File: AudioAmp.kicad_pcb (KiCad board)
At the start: 2 copper layers, 134 x 38 mm, 56 parts, among them J1 ACJS-MHOM, J2 ACJS-MHOM, Q1 MJE182G, Q12 MMBT5401, Q13 MMBT5401, Q2 MJE172G, Q3 MMBT5551(RANGE:200-300), Q9 MMBT5551(RANGE:200-300)

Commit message: PCB fertig gemacht.
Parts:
- removed H6: VCC _GND, MountingHole:MountingHole_2.5mm_Pad
- moved TP8 130.4 mm to (195.0, 92.8)
- moved TP10 101.7 mm to (151.4, 123.2)
- moved H3 97.3 mm to (175.2, 92.5)
- moved H4 93.5 mm to (166.0, 123.0)
- moved D10 83.8 mm to (170.3, 110.9), turned to 180 degrees
- moved C9 80.7 mm to (162.3, 91.0), turned to 180 degrees
- moved R12 78.5 mm to (176.5, 119.5)
- moved C2 75.6 mm to (171.7, 117.6), turned to -90 degrees
- moved TP5 70.5 mm to (156.8, 91.0)
- moved R10 70.3 mm to (119.0, 115.0)
- moved C4 69.1 mm to (151.4, 119.2), turned to 90 degrees
- moved J2 67.7 mm to (182.3, 101.1)
- moved R15 66.4 mm to (113.5, 122.5)
- moved C7 65.6 mm to (112.0, 113.0)
- moved R9 64.7 mm to (113.5, 117.0)
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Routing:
- net Net-(C1-Pad2): track 115.0 -> 28.7 mm
- net Net-(D10-A): track 12.4 -> 90.3 mm, vias 0 -> 4
- net Net-(D1-A): track 68.2 -> 128.5 mm, vias 0 -> 2
- net Net-(D9-K): track 19.2 -> 64.2 mm
- net Net-(Q13-C): track 19.7 -> 64.0 mm
- net Net-(D1-K): track 4.68 -> 43.8 mm
- net Net-(D4-A): track 0.00 -> 37.4 mm
- net Net-(Q12-E): track 14.3 -> 35.5 mm, vias 0 -> 2
- net Net-(H1-Pad1): track 28.5 -> 8.61 mm
- net Net-(D2-K): track 9.26 -> 21.0 mm
- net Net-(Q3-B): track 0.00 -> 10.2 mm
- net Net-(D2-A): track 35.3 -> 25.3 mm
- net Net-(Q9-E): track 0.00 -> 8.83 mm
- net Net-(Q1-E): track 4.50 -> 13.2 mm
- net Net-(C6-Pad1): track 13.2 -> 6.86 mm
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- added copper zone on B.Cu, net Net-(C1-Pad2)
- added copper zone on F.Cu, net Net-(C1-Pad2)
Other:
- board size 134 x 38 mm -> 145 x 40 mm

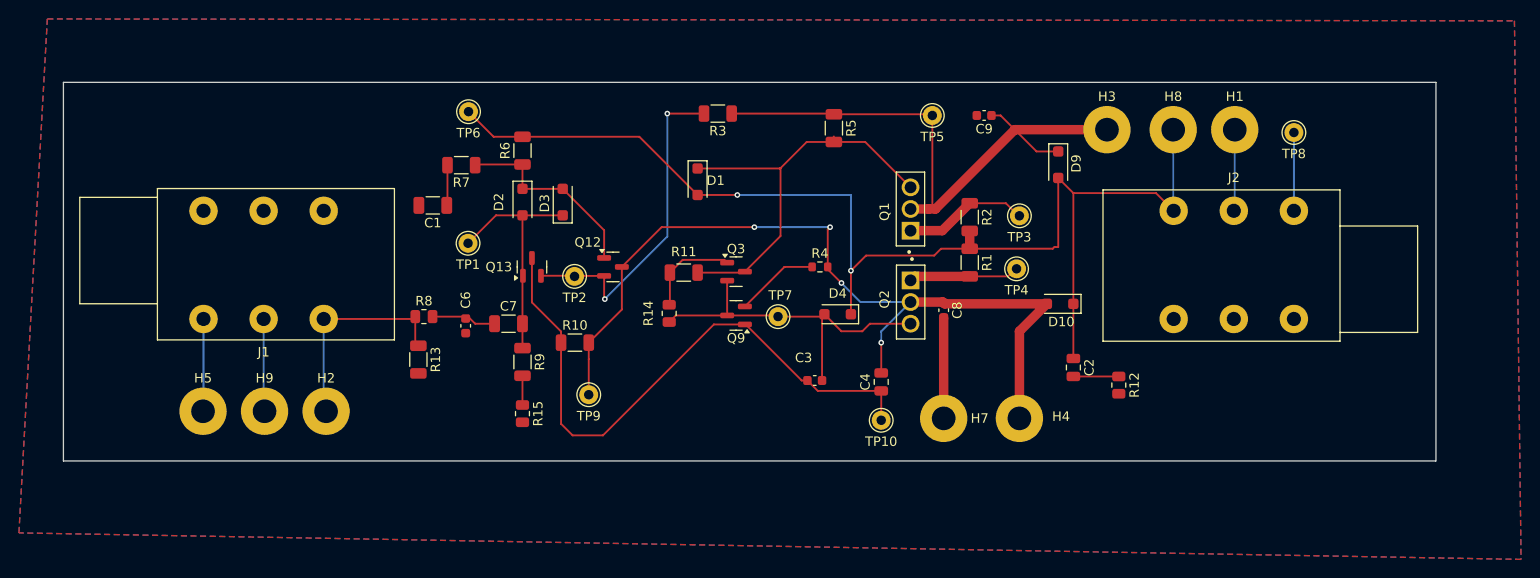
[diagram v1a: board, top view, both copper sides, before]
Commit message: CHA: Leitung zu Hochstrom erhöht
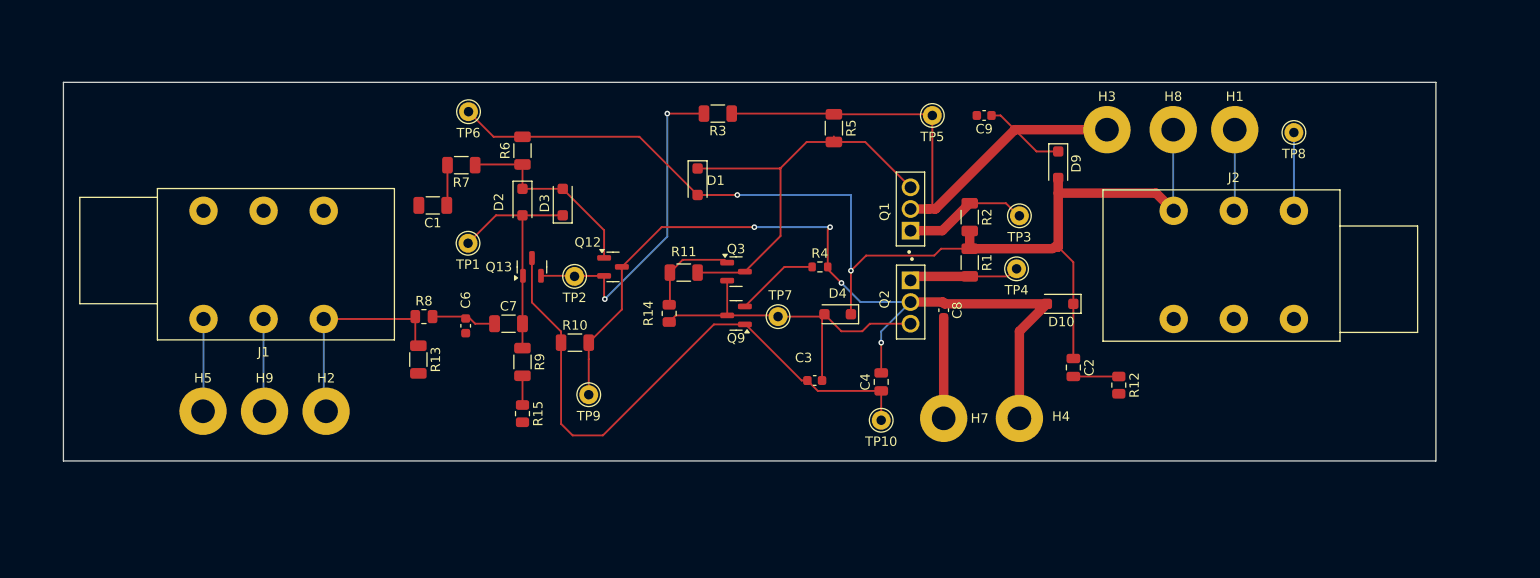
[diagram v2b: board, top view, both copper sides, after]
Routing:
- net Net-(D1-A): track 128.5 -> 122.8 mm
- removed copper zone on B.Cu, net Net-(C1-Pad2)
- removed copper zone on F.Cu, net Net-(C1-Pad2)
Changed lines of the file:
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@@
 		(start 169.525 105.075)
 		(end 160.75 105.075)
-		(width 0.2)
+		(width 1)
 		(layer "F.Cu")
 		(net 4)
@@
 	)
 	(segment
+		(start 171.7 106.5)
+		(end 170.1 104.9)
+		(width 0.2)
+		(layer "F.Cu")
+		(net 4)
+	)
+	(segment
 		(start 170.1 97.6)
 		(end 170.1 104.9)
-		(width 0.2)
+		(width 1)
 		(layer "F.Cu")
 		(net 4)
@@
 		(start 182.3 101.07)
 		(end 180.43 99.2)
-		(width 0.2)
+		(width 1)
 		(layer "F.Cu")
 		(net 4)
@@
 	)
 	(segment
-		(start 180.43 99.2)
-		(end 171.7 99.2)
-		(width 0.2)
-		(layer "F.Cu")
-		(net 4)
-	)
-	(segment
 		(start 113.5 93.25)
 		(end 110.45 93.25)
@@
 	)
 	(segment
-		(start 171.7 99.2)
-		(end 170.1 97.6)
-		(width 0.2)
-		(layer "F.Cu")
-		(net 4)
-	)
-	(segment
 		(start 132 99.4)
 		(end 136.2 99.4)
@@
 	)
 	(segment
+		(start 180.43 99.2)
+		(end 170.1 99.2)
+		(width 1)
+		(layer "F.Cu")
+		(net 4)
+	)
+	(segment
 		(start 157.725 105.075)
 		(end 160.75 105.075)
@@
 	)
 	(segment
-		(start 171.7 110.9)
-		(end 171.7 99.2)
-		(width 0.2)
-		(layer "F.Cu")
-		(net 4)
-	)
-	(segment
 		(start 160.75 103.2)
 		(end 160.75 105.075)
@@
 	)
 	(segment
+		(start 171.7 110.9)
+		(end 171.7 106.5)
+		(width 0.2)
+		(layer "F.Cu")
+		(net 4)
+	)
+	(segment
 		(start 170.1 104.9)
 		(end 169.7 104.9)
-		(width 0.2)
+		(width 1)
 		(layer "F.Cu")
 		(net 4)
@@
 		(net 27)
 	)
-	(zone
-		(net 2)
-		(net_name "Net-(C1-Pad2)")
-		(layers "F.Cu" "B.Cu")
-		(hatch edge 0.5)
-		(connect_pads
-			(clearance 0.5)
-		)
-		(min_thickness 0.25)
-		(filled_areas_thickness no)
-		(fill yes
-			(thermal_gap 0.5)
-			(thermal_bridge_width 0.5)
-		)
-		(polygon
-			(pts
-				(xy 63.3 80.8) (xy 218.3 81) (xy 219 137.9) (xy 60.3 135.1)
-			)
-		)
-	)
 	(embedded_fonts no)

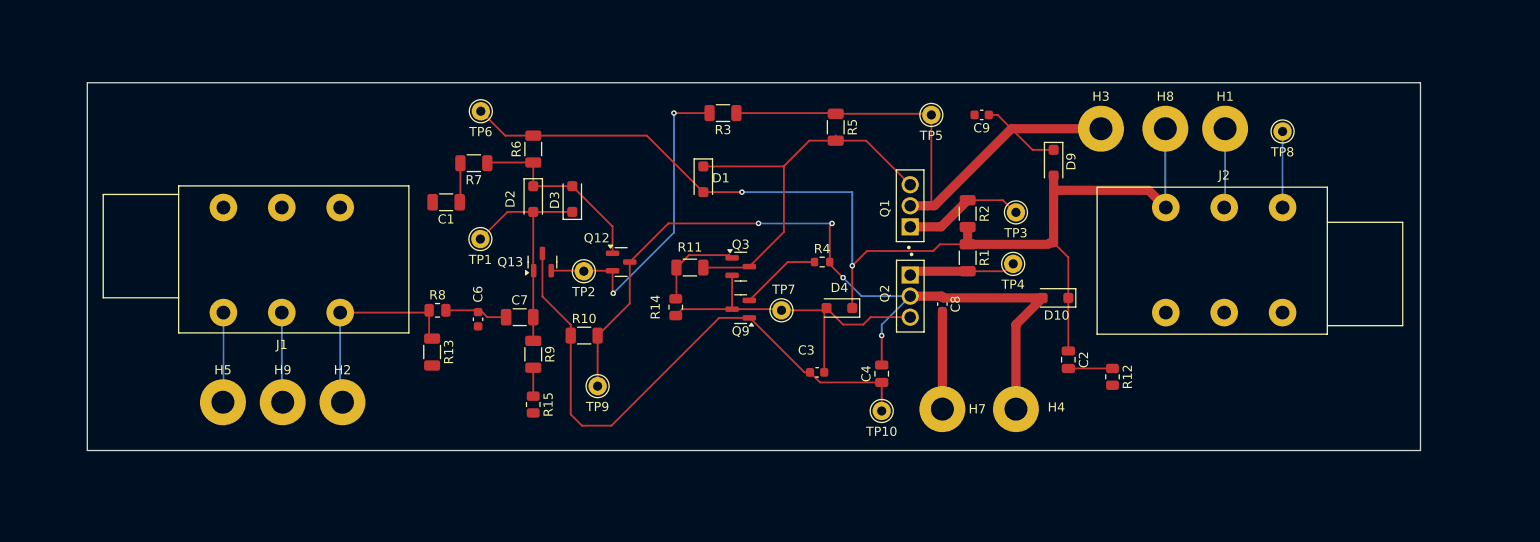
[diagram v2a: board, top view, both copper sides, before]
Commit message: Neues GND Netz gesetz und angeschlossen, Planinen rev hinzugefügt
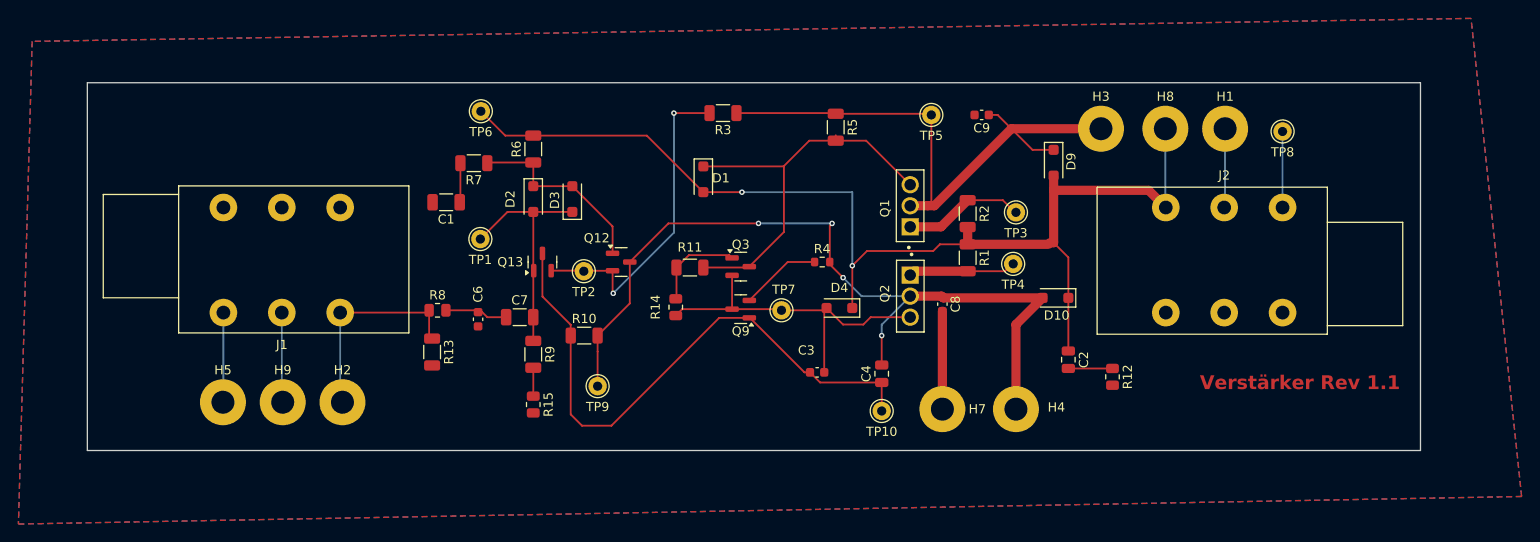
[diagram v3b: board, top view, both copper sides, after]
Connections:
- net Net-(C1-Pad2) renamed /GND
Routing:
- added copper zone on B.Cu, net /GND
- added copper zone on F.Cu, net /GND
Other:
- board text added: "Verstärker Rev 1.1"
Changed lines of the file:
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@@
 	(net 0 "")
 	(net 1 "Net-(C1-Pad1)")
-	(net 2 "Net-(C1-Pad2)")
+	(net 2 "/GND")
 	(net 3 "Net-(C2-Pad2)")
 	(net 4 "Net-(D1-A)")
@@
 			(layers "*.Cu" "*.Mask")
 			(remove_unused_layers no)
-			(net 2 "Net-(C1-Pad2)")
+			(net 2 "/GND")
 			(pinfunction "1")
 			(pintype "passive")
@@
 			(layers "F.Cu" "F.Mask" "F.Paste")
 			(roundrect_rratio 0.222222)
-			(net 2 "Net-(C1-Pad2)")
+			(net 2 "/GND")
 			(pintype "passive")
 		)
@@
 			(layers "F.Cu" "F.Mask" "F.Paste")
 			(roundrect_rratio 0.243902)
-			(net 2 "Net-(C1-Pad2)")
+			(net 2 "/GND")
 			(pintype "passive")
 		)
@@
 			(layers "*.Cu" "*.Mask")
 			(remove_unused_layers no)
-			(net 2 "Net-(C1-Pad2)")
+			(net 2 "/GND")
 			(pinfunction "1")
 			(pintype "input")
@@
 			(layers "F.Cu" "F.Mask" "F.Paste")
 			(roundrect_rratio 0.25)
-			(net 2 "Net-(C1-Pad2)")
+			(net 2 "/GND")
 			(pintype "passive")
 		)
@@
 			(layers "*.Cu" "*.Mask")
 			(remove_unused_layers no)
-			(net 2 "Net-(C1-Pad2)")
+			(net 2 "/GND")
 			(pinfunction "1")
 			(pintype "input")
@@
 			(layers "F.Cu" "F.Mask" "F.Paste")
 			(roundrect_rratio 0.25)
-			(net 2 "Net-(C1-Pad2)")
+			(net 2 "/GND")
 			(pintype "passive")
 		)
@@
 			(layers "F.Cu" "F.Mask" "F.Paste")
 			(roundrect_rratio 0.217391)
-			(net 2 "Net-(C1-Pad2)")
+			(net 2 "/GND")
 			(pintype "passive")
 		)
@@
 			(layers "F.Cu" "F.Mask" "F.Paste")
 			(roundrect_rratio 0.243902)
-			(net 2 "Net-(C1-Pad2)")
+			(net 2 "/GND")
 			(pintype "passive")
 		)
@@
 			(layers "*.Cu" "*.Mask")
 			(remove_unused_layers no)
-			(net 2 "Net-(C1-Pad2)")
+			(net 2 "/GND")
 			(pintype "passive")
 		)
@@
 			(layers "F.Cu" "F.Mask" "F.Paste")
 			(roundrect_rratio 0.25)
-			(net 2 "Net-(C1-Pad2)")
+			(net 2 "/GND")
 			(pintype "passive")
 		)
@@
 			(layers "*.Cu" "*.Mask")
 			(remove_unused_layers no)
-			(net 2 "Net-(C1-Pad2)")
+			(net 2 "/GND")
 			(pintype "passive")
 		)
@@
 		(layer "Edge.Cuts")
 	)
+	(gr_text "Verstärker Rev 1.1"
+		(at 186 121 0)
+		(layer "F.Cu")
+		(effects
+			(font
+				(size 1.5 1.5)
+				(thickness 0.3)
+				(bold yes)
+			)
+			(justify left bottom)
+		)
+	)
 	(gr_text "In"
 		(at 82.7125 108.0375 90)
@@
 		(net 27)
 	)
+	(zone
+		(net 2)
+		(net_name "/GND")
+		(layers "F.Cu" "B.Cu")
+		(hatch full 0.5)
+		(connect_pads
+			(clearance 0.5)
+		)
+		(min_thickness 0.25)
+		(filled_areas_thickness no)
+		(fill yes
+			(thermal_gap 0.5)
+			(thermal_bridge_width 0.5)
+		)
+		(polygon
+			(pts
+				(xy 59 83) (xy 57.5 135.5) (xy 221 132.5) (xy 215.5 80.5)
+			)
+		)
+	)
 	(embedded_fonts no)

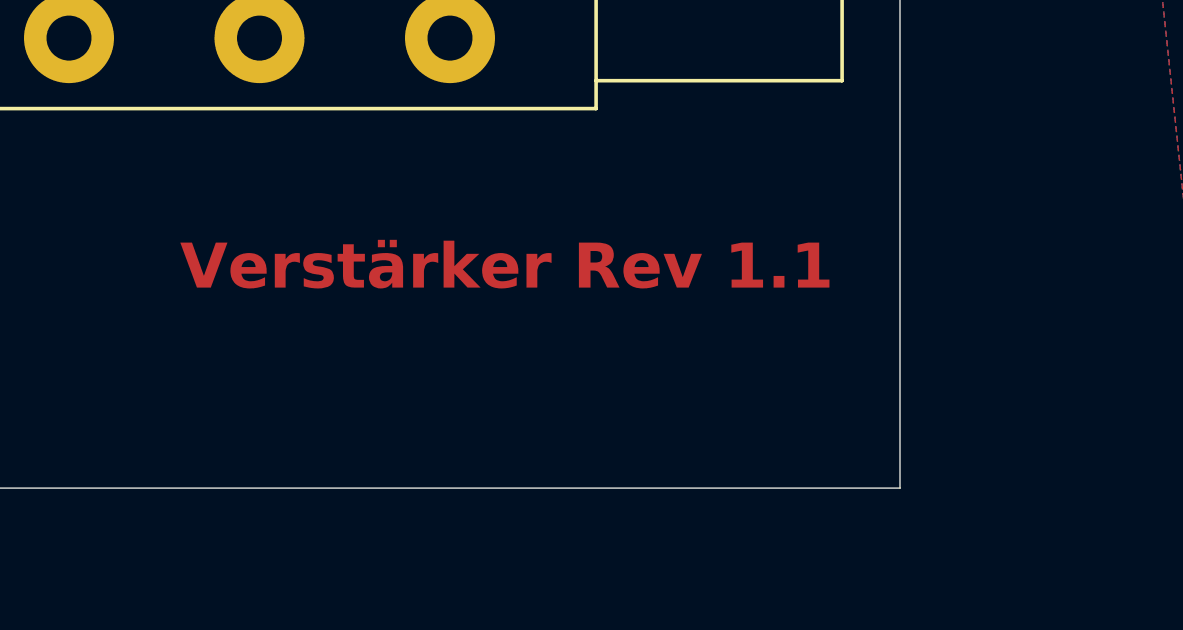
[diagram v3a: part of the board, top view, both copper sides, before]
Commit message: CHA: Projektdaten ergänzt
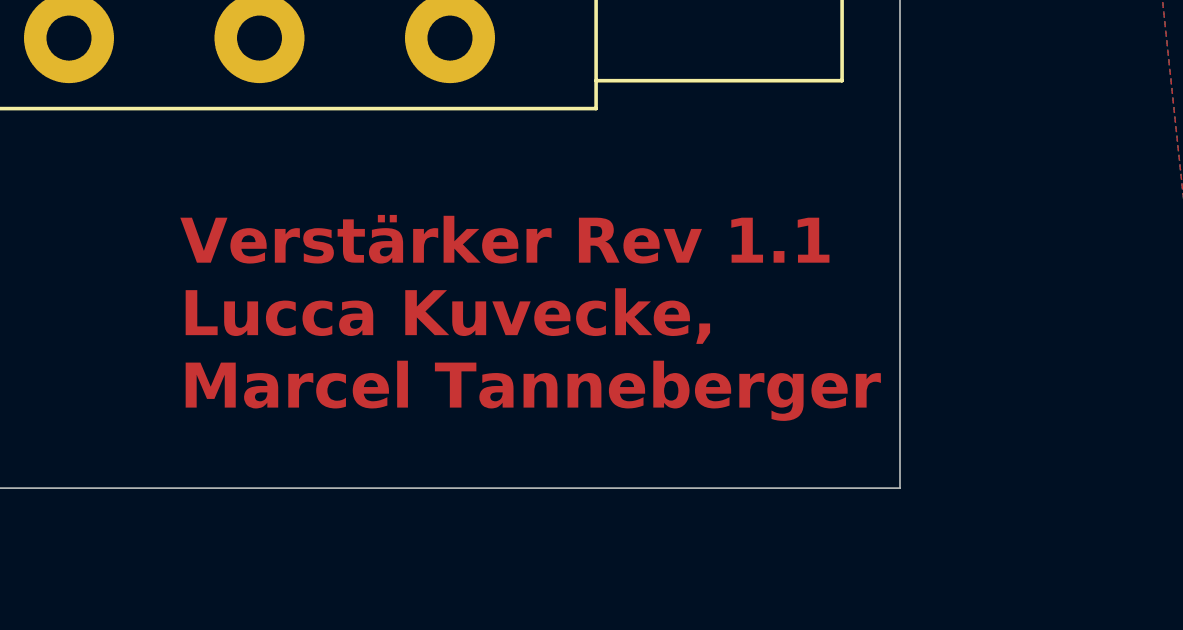
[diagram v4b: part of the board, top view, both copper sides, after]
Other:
- board text added: "Verstärker Rev 1.1 Lucca Kuvecke, Marcel Tanneberger"
- board text removed: "Verstärker Rev 1.1"
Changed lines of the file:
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@@
 		(layer "Edge.Cuts")
 	)
-	(gr_text "Verstärker Rev 1.1"
-		(at 186 121 0)
+	(gr_text "Verstärker Rev 1.1\nLucca Kuvecke,\nMarcel Tanneberger"
+		(at 186 125 0)
 		(layer "F.Cu")
 		(effects
